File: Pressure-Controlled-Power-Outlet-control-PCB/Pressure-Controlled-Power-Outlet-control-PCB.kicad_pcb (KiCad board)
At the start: 4 copper layers, 100.3 x 86.4 mm, 39 parts, among them J1 pressure sensor, J2 1017514, J3 I2C0 Connector, J4 SPI1 Connector, J5 FanA 5V/24V, J6 FanB 5V/24V, K1 T9GV5L24-24, K2 T9GV5L24-24, M1 Fan_4pin, M2 Fan_4pin, Q1 2N3906, Q2 IRF540N, Q3 IRF540N, Q4 2N3906, Q5 2N3904, Q6 2N3904, U1 Pico, U2 LM324, U3 LF50_TO220

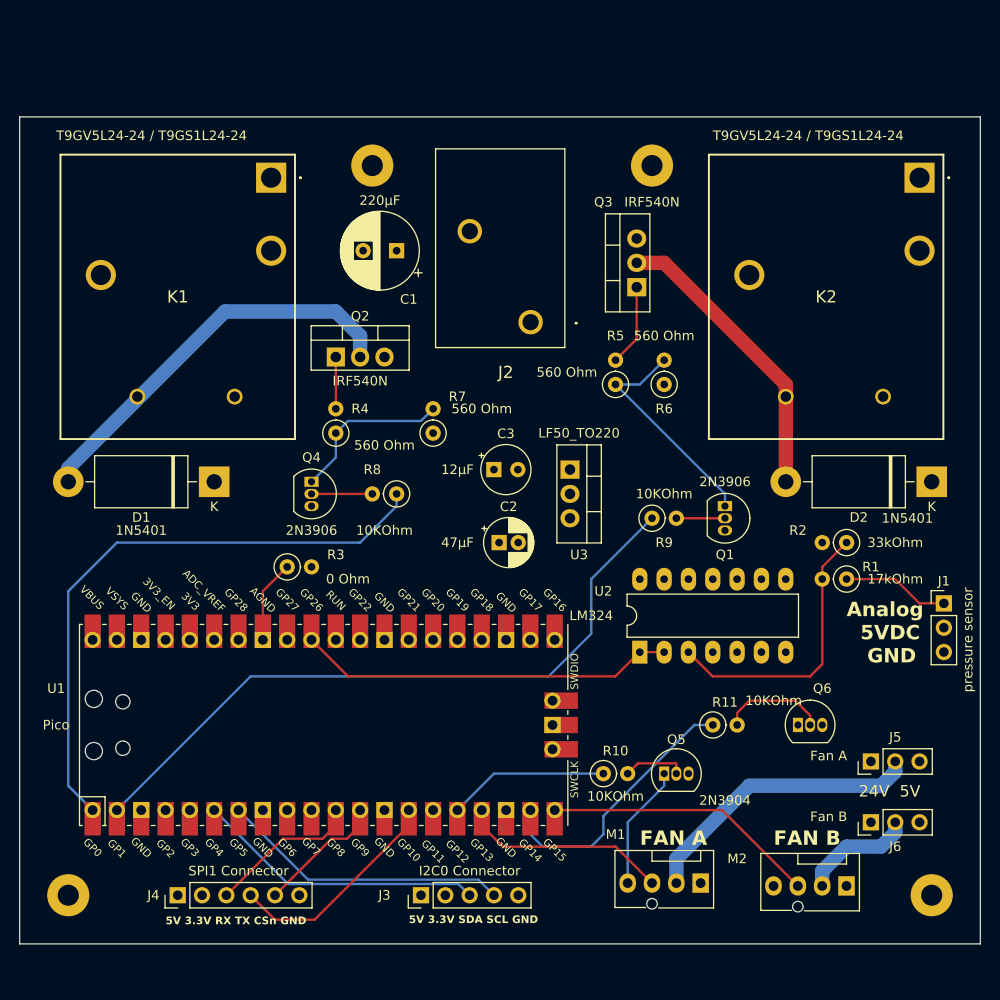
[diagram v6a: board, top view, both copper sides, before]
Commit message: redid the fan controllers
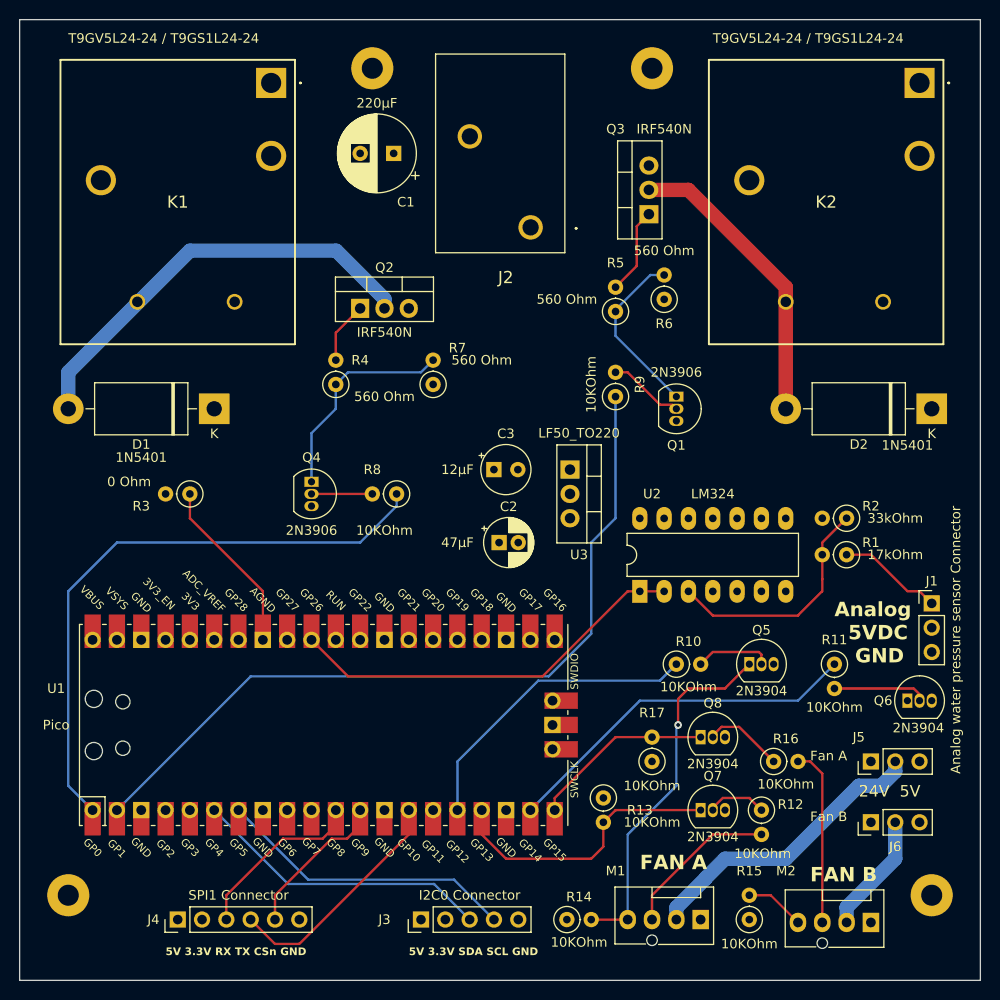
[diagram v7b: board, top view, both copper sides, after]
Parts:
- added Q7: 2N3904, Package_TO_SOT_THT:TO-92_Inline, F.Cu at (157.5, 138.4)
- added Q8: 2N3904, Package_TO_SOT_THT:TO-92_Inline, F.Cu at (157.5, 130.8)
- added R12: 10KOhm, Resistor_THT:R_Axial_DIN0207_L6.3mm_D2.5mm_P2.54mm_Vertical, F.Cu at (163.8, 138.4)
- added R13: 10KOhm, Resistor_THT:R_Axial_DIN0207_L6.3mm_D2.5mm_P2.54mm_Vertical, F.Cu at (147.3, 137.2)
- added R14: 10KOhm, Resistor_THT:R_Axial_DIN0207_L6.3mm_D2.5mm_P2.54mm_Vertical, F.Cu at (143.5, 149.9)
- added R15: 10KOhm, Resistor_THT:R_Axial_DIN0207_L6.3mm_D2.5mm_P2.54mm_Vertical, F.Cu at (162.6, 149.9)
- added R16: 10KOhm, Resistor_THT:R_Axial_DIN0207_L6.3mm_D2.5mm_P2.54mm_Vertical, F.Cu at (165.1, 133.3)
- added R17: 10KOhm, Resistor_THT:R_Axial_DIN0207_L6.3mm_D2.5mm_P2.54mm_Vertical, F.Cu at (152.4, 133.3)
- J1: value pressure sensor -> Analog water pressure sensor Connector
- moved Q5 14.5 mm to (162.6, 123.2)
- moved R11 14.2 mm to (171.4, 123.2), turned to -90 degrees
- moved R10 13.7 mm to (154.9, 123.2)
- moved R9 13.3 mm to (148.6, 95.2), turned to 90 degrees
- moved R3 12.7 mm to (104.1, 105.4), turned to 180 degrees
- moved Q1 12.5 mm to (154.9, 95.2)
- moved Q6 11.7 mm to (179.1, 127.0)
- moved C1 10.2 mm to (125.4, 69.8)
- moved H3 10.2 mm to (152.4, 61.0)
- moved H4 10.2 mm to (123.2, 61.0)
- moved K1 9.90 mm to (112.6, 62.5)
- moved K2 9.90 mm to (180.3, 62.5)
- moved J2 9.90 mm to (139.7, 77.6)
- moved R6 8.89 mm to (153.7, 85.1)
- moved Q3 7.73 mm to (152.1, 76.2)
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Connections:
- M1 pad 3: /FanA_Tac -> Net-(M1-Tacho)
- M2 pad 3: /FanB_Tac -> Net-(M2-Tacho)
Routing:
- net +3.3V: track 75.2 -> 125.1 mm
- net Net-(M1-PWM): track 13.0 -> 38.0 mm, vias 0 -> 1
- net Net-(M2-Tacho): track 0.00 -> 18.6 mm
- net Net-(M2-PWM): track 17.9 -> 34.9 mm
- net Net-(M1-Tacho): track 0.00 -> 16.6 mm
- net /FanA_PWM: track 16.8 -> 32.1 mm
- net /Activate_Neutral: track 71.9 -> 83.0 mm
- net +5V: track 0.00 -> 11.0 mm
- net Net-(U1-AGND): track 8.67 -> 18.4 mm
- net /FanB_PWM: track 28.5 -> 38.1 mm
- net /FanB_Tac: track 28.7 -> 19.1 mm
- net Net-(Q8-B): track 0.00 -> 8.38 mm
- net /FanA_Tac: track 21.9 -> 30.0 mm
- net +24V: track 38.2 -> 45.8 mm
- net Net-(Q7-B): track 0.00 -> 6.26 mm
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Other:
- board size 100.3 x 86.4 mm -> 100.3 x 100.3 mm
- board text added: "2N3904"

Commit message: welp moved some stuff around
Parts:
- moved Q8 11.7 mm to (148.6, 123.2)
- moved R16 8.13 mm to (158.8, 128.3)
- moved U2 7.41 mm to (147.3, 109.2)
- moved C2 6.89 mm to (129.5, 110.5)
- moved U3 6.35 mm to (137.5, 102.9)
- moved C3 6.31 mm to (129.6, 102.9)
- moved Q5 5.24 mm to (163.8, 118.1)
- moved Q4 5.08 mm to (111.8, 104.1)
- moved R10 5.08 mm to (154.9, 118.1)
- moved R8 5.08 mm to (120.7, 105.4)
- moved Q1 4.02 mm to (153.7, 91.4)
- moved R5 3.81 mm to (144.8, 86.4)
- moved R12 2.84 mm to (165.1, 135.9)
- moved R17 1.80 mm to (151.1, 132.1)
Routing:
- net Net-(M2-Tacho): track 18.6 -> 29.3 mm
- net +5V: track 11.0 -> 20.9 mm
- net +3.3V: track 125.1 -> 133.7 mm
- net /Activate_Live: track 63.2 -> 57.3 mm
- net Net-(M1-PWM): track 38.0 -> 42.8 mm
- net /ADC0: track 42.1 -> 46.1 mm
- net Net-(Q3-G): track 9.06 -> 12.9 mm
- net Net-(Q4-E): track 22.4 -> 26.0 mm
- net Net-(Q1-E): track 18.3 -> 21.5 mm
- net Net-(Q5-B): track 7.99 -> 11.1 mm
- net Net-(Q1-B): track 7.93 -> 5.08 mm
- net Net-(Q8-B): track 8.38 -> 11.1 mm
- net Net-(M1-Tacho): track 16.6 -> 18.9 mm
- net /FanA_PWM: track 32.1 -> 34.3 mm
- net /FanB_Tac: track 19.1 -> 20.7 mm
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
